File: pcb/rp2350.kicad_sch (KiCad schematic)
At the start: 50 parts, among them J2 USB_C_Receptacle_USB2.0_16P, J3 Conn_01x14_Pin, J9 Conn_01x03_Pin, SW1 SW_Push, SW2 SW_DIP_x04, SW3 SW_Push, U1 W25Q32JVSS, U2 NUP2202, U3 RP2350, U4 LM4040C33FTA, Y1 12Mhz

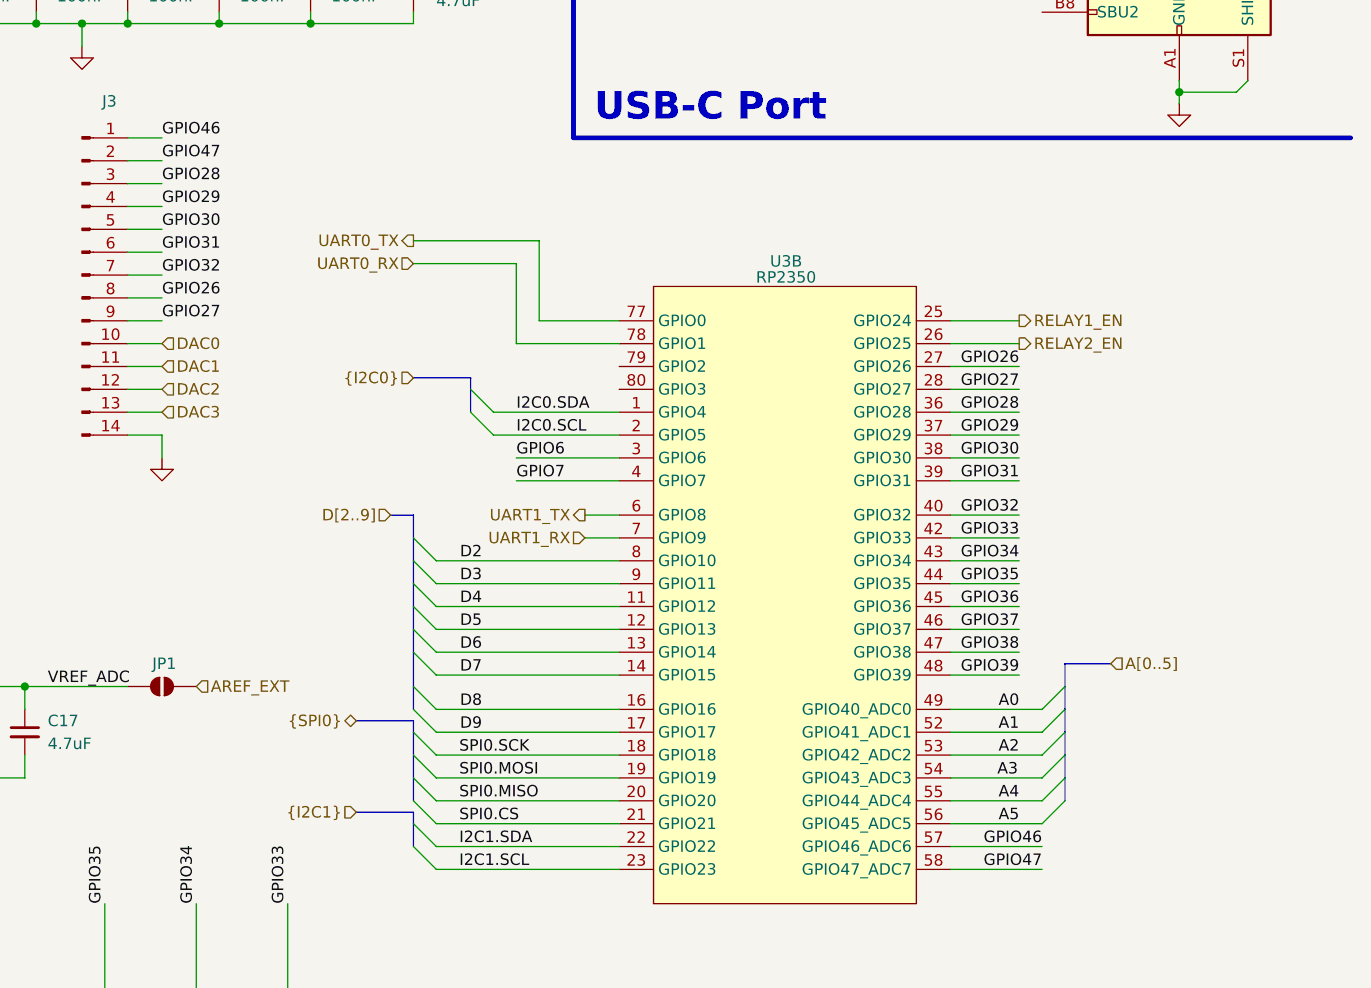
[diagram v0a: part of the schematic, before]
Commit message: Added gerbers, added 2x3 Arduino header.
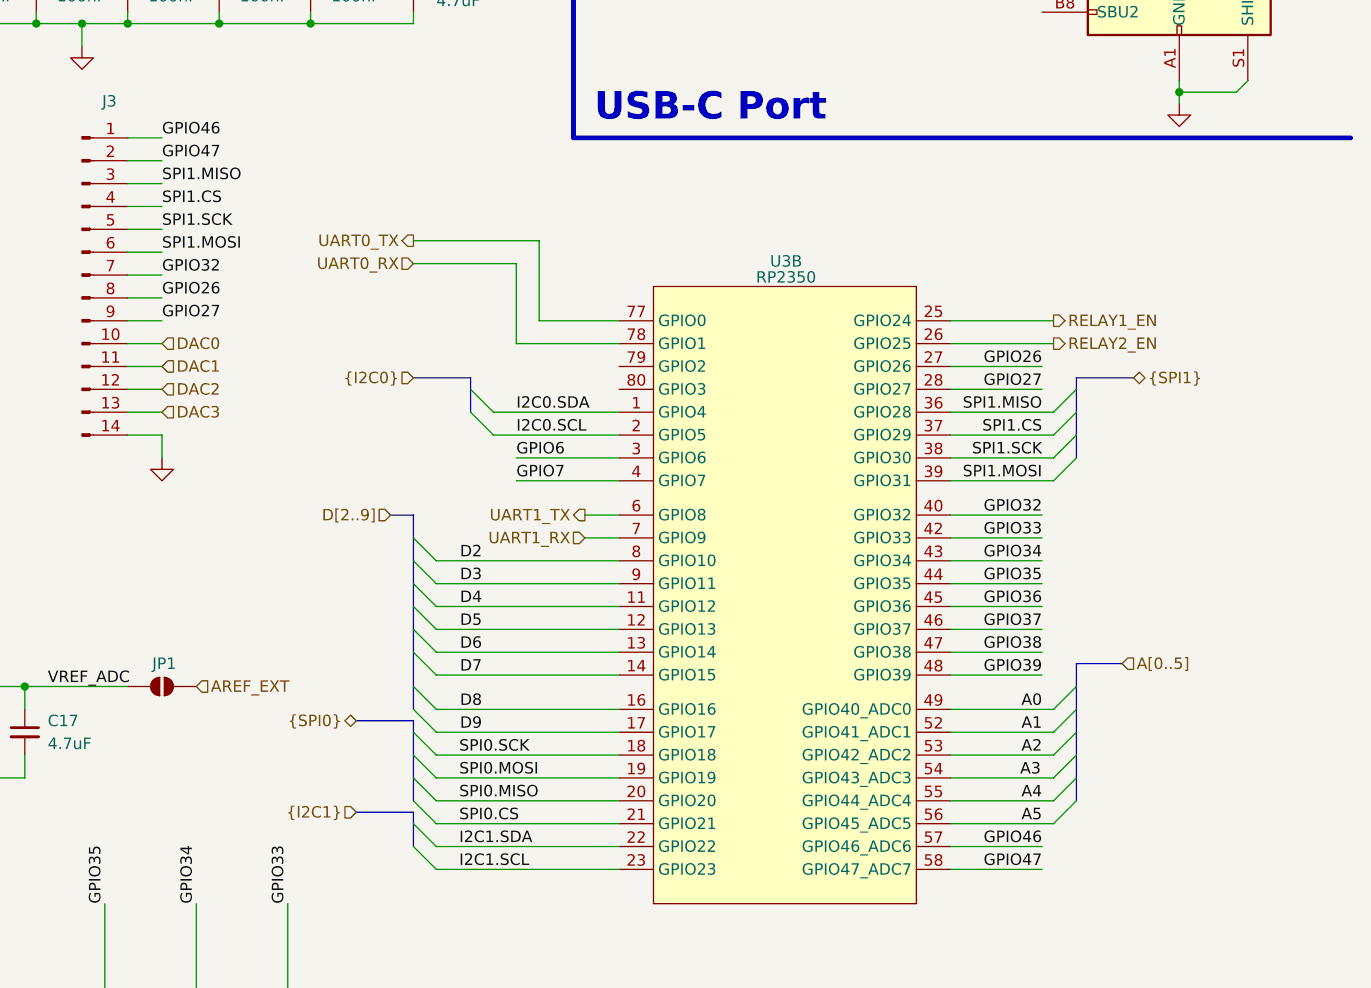
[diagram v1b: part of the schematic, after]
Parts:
- C18, C19: MPN (none) -> GJM1555C1H150GB01D
- D4: MPN (none) -> LTST-C190KRKT
- D5: MPN (none) -> LTST-C190GKT
- D6: MPN (none) -> LTST-C190KSKT
- R6: MPN (none) -> RC0402FR-070RL
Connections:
- net GPIO28 renamed SPI1.MISO
- net GPIO29 renamed SPI1.CS
- net GPIO30 renamed SPI1.SCK
- net GPIO31 renamed SPI1.MOSI

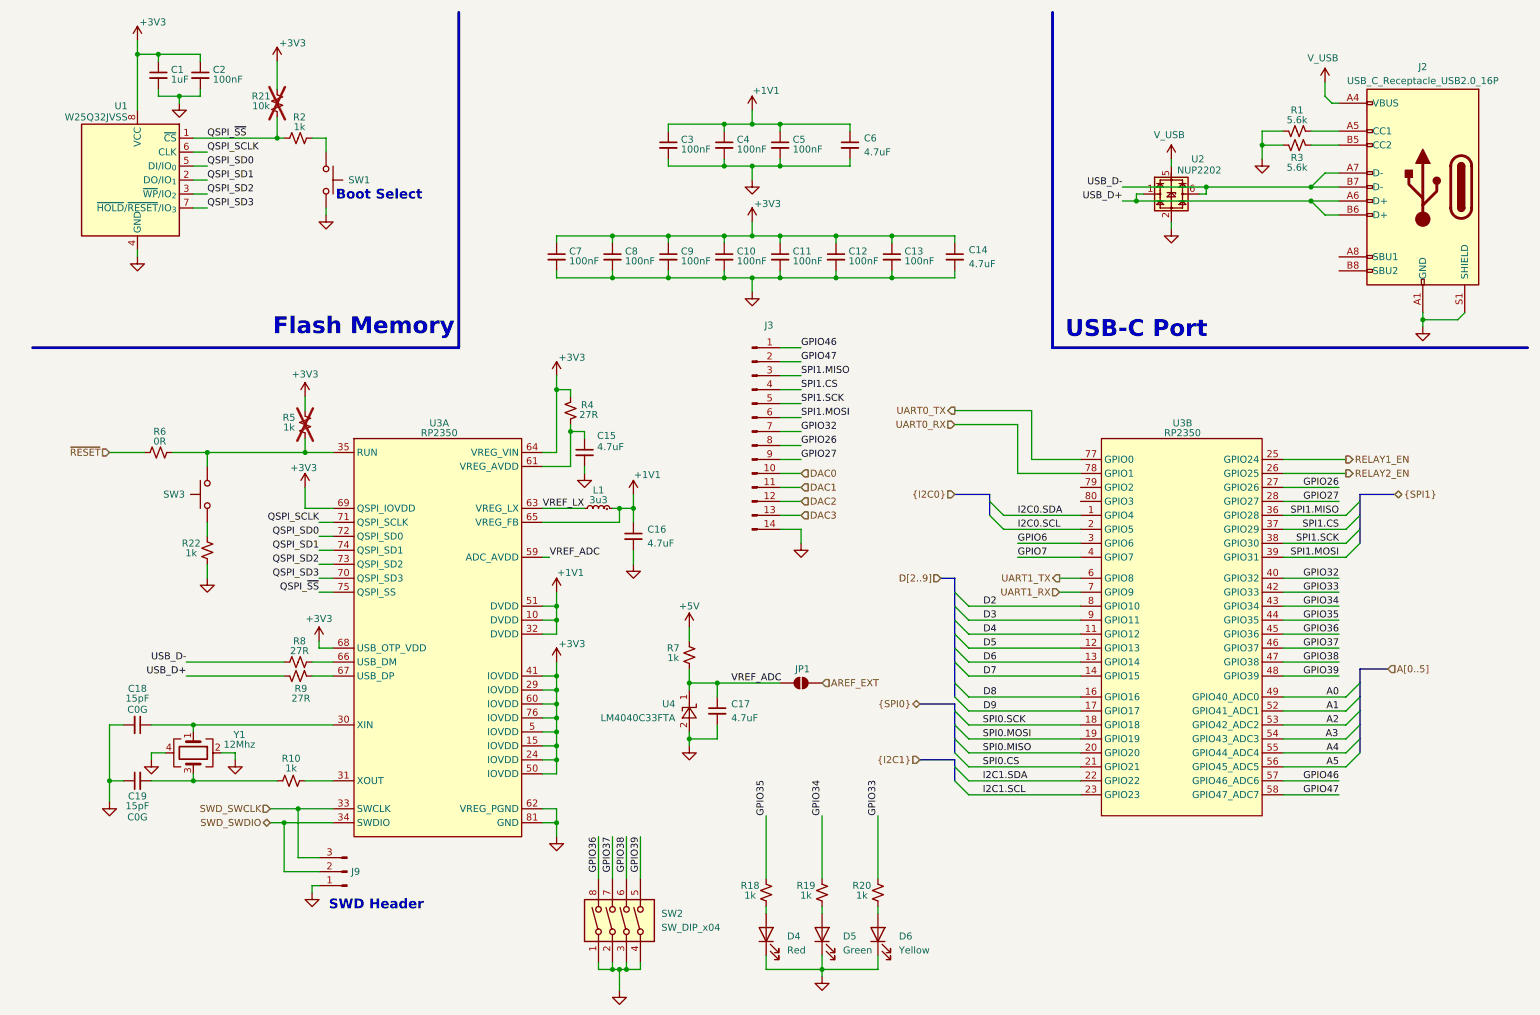
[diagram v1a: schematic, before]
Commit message: Added remaining part numbers, removed silk for holes, minor touchups
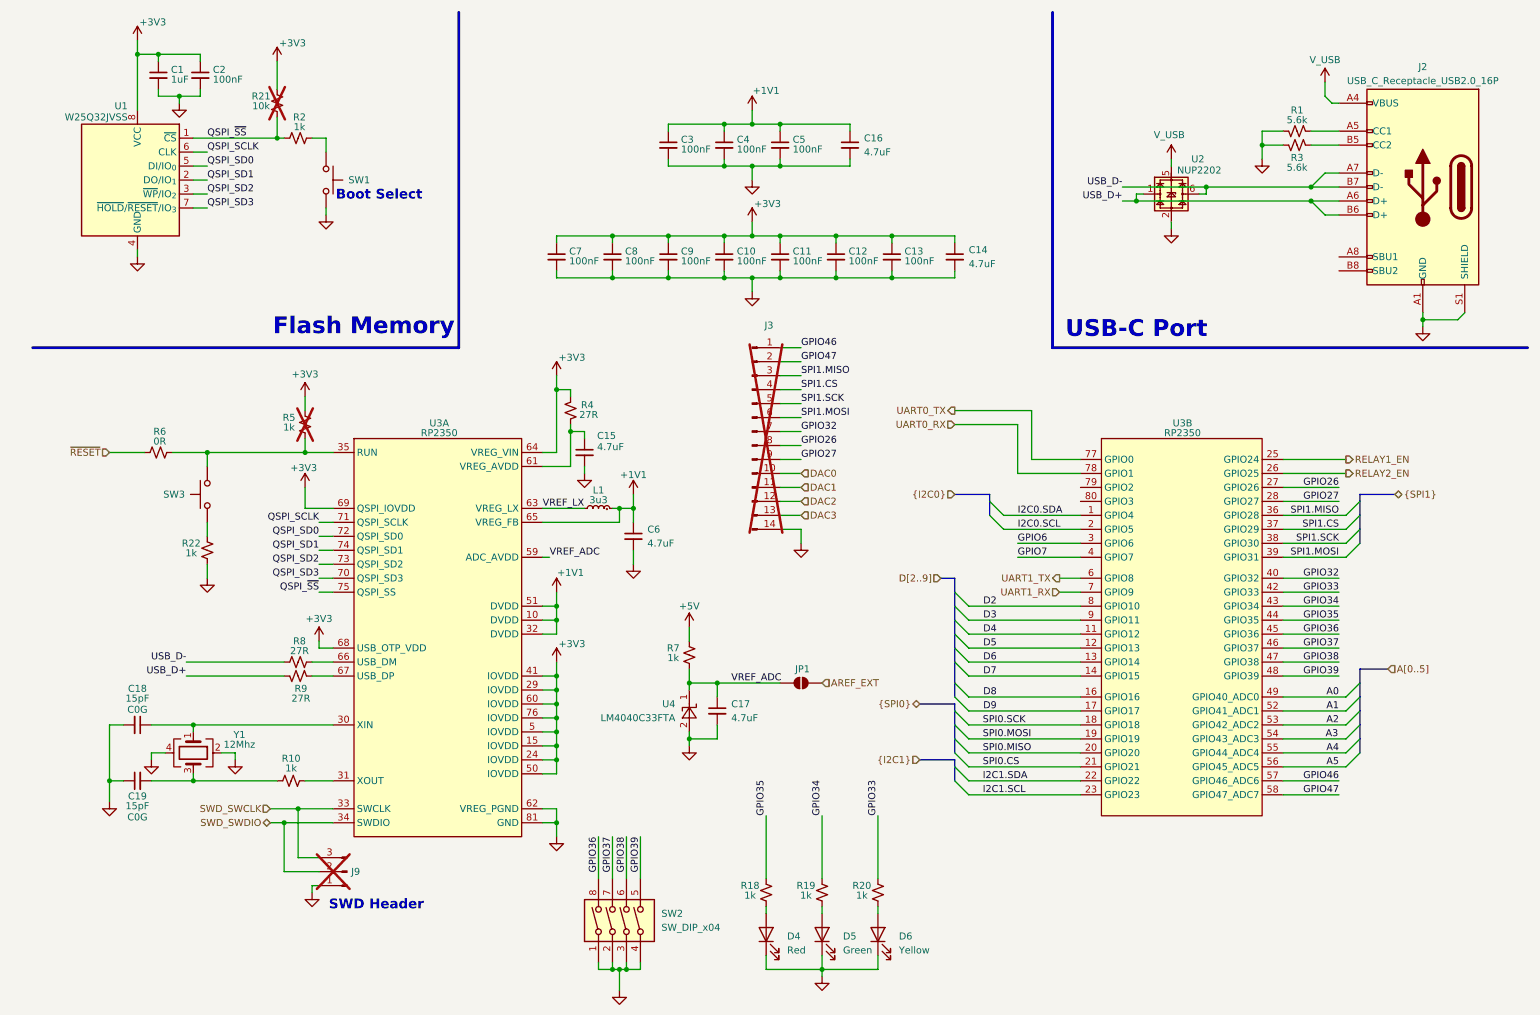
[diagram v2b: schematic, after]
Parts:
- J3: MPN (none) -> 77311-101-14LF; now not fitted
- J9: now not fitted; now left out of the parts list
- U1: MPN (none) -> W25Q32JVSSIQ
- renumbered C6 to C16, C16 to C6
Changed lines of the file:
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@@
 		)
 		(property "Value" "+1V1"
-			(at 124.46 96.774 0)
+			(at 121.92 96.774 0)
 			(effects
 				(font
@@
 			)
 		)
+		(property "MPN" "W25Q32JVSSIQ"
+			(at 31.75 43.18 0)
+			(effects
+				(font
+					(size 1.27 1.27)
+				)
+				(hide yes)
+			)
+		)
 		(pin "8"
 		)
@@
 		(dnp no)
 		(fields_autoplaced yes)
-		(property "Reference" "C6"
+		(property "Reference" "C16"
 			(at 163.83 35.5662 0)
 			(effects
@@
 			(project "blocky_breakout_pcb"
 				(path "/deaf739e-0e27-4f2f-890a-6dd284a38e9f/070b8cc2-3998-46de-84e2-c30831f55ad5"
-					(reference "C6")
+					(reference "C16")
 					(unit 1)
 				)
@@
 		(unit 1)
 		(exclude_from_sim no)
-		(in_bom yes)
+		(in_bom no)
 		(on_board yes)
-		(dnp no)
+		(dnp yes)
 		(property "Reference" "J9"
 			(at 70.612 168.91 0)
@@
 		(dnp no)
 		(fields_autoplaced yes)
-		(property "Reference" "C16"
+		(property "Reference" "C6"
 			(at 124.46 106.6862 0)
 			(effects
@@
 			(project ""
 				(path "/deaf739e-0e27-4f2f-890a-6dd284a38e9f/070b8cc2-3998-46de-84e2-c30831f55ad5"
-					(reference "C16")
+					(reference "C6")
 					(unit 1)
 				)
@@
 		)
 		(property "Value" "V_USB"
-			(at 247.269 21.0058 0)
+			(at 247.65 21.336 0)
 			(effects
 				(font
@@
 		(in_bom yes)
 		(on_board yes)
-		(dnp no)
+		(dnp yes)
 		(property "Reference" "J3"
 			(at 146.558 69.596 0)
@@
 			(at 143.51 88.9 0)
 			(effects
+				(font
+					(size 1.27 1.27)
+				)
+				(hide yes)
+			)
+		)
+		(property "MPN" "77311-101-14LF"
+			(at 143.51 88.9 0)
+			(effects

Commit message: R0.1 released
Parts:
- renumbered C6 to C16, C16 to C6, D4 to D1, D5 to D2, D6 to D3, J2 to J1, J3 to J2, J9 to J3, R21 to R1, R8 to R10, R9 to R11, R10 to R12, R18 to R13, R19 to R14, R20 to R15, R1 to R2, R2 to R3, R3 to R4, R4 to R5, R5 to R6, R6 to R7, R22 to R8, R7 to R9, SW3 to SW2, SW2 to SW3
